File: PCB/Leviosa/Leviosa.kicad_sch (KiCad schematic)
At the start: 48 parts, among them J1 2.54mm 1x03 Servo 1, J2 2.54mm 1x03 Servo 1, J3 2.54mm 1x03 Spare, J4 Barrel_Jack, Q3 TIP122, Q4 TIP122, U1 LM324, U2 ATtiny13A-P, U3 TPS1H200AQDGNRQ1, U5 L7805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

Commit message: Update PCB
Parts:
- Schottky1: renamed from SR206-TPCT-ND1; value Schottky Diode -> Schottky Diode SR206-TPCT-ND1
- renumbered EMcoil1 to Coil1, RV1_10k_Pot1 to Pot1, RV2_10k_Pot1 to Pot2
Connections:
- net at Pot2.1: now also R5.2; no longer R4.1
- net at Pot2.3: now also R4.1; no longer R5.2
- net at R3.2: now also Pot1.3; no longer Pot1.1
- net at R2.1: now also Pot1.1; no longer Pot1.3
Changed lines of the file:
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@@
 	(wire
 		(pts
-			(xy 41.91 38.1) (xy 41.91 39.37)
-		)
-		(stroke
-			(width 0)
-			(type default)
-		)
-	)
-	(wire
-		(pts
 			(xy 219.71 57.15) (xy 245.11 57.15)
 		)
@@
 	(wire
 		(pts
+			(xy 41.91 38.1) (xy 41.91 39.37)
+		)
+		(stroke
+			(width 0)
+			(type default)
+		)
+	)
+	(wire
+		(pts
 			(xy 60.96 55.88) (xy 76.2 55.88)
 		)
@@
 		(lib_id "Device:R_Potentiometer_US")
 		(at 161.29 92.71 0)
+		(mirror x)
 		(unit 1)
 		(exclude_from_sim no)
@@
 		(on_board yes)
 		(dnp no)
-		(property "Reference" "RV2_10k_Pot1"
-			(at 153.162 91.694 0)
+		(property "Reference" "Pot2"
+			(at 153.162 93.726 0)
 			(effects
 				(font
@@
 		)
 		(property "Value" "3362S-1-103LF"
-			(at 151.892 93.98 0)
+			(at 151.892 91.44 0)
 			(effects
 				(font
@@
 			)
 		)
-		(property "Description" ""
-			(at 161.29 92.71 0)
+		(property "Description" "10k pot"
+			(at 166.624 94.234 0)
 			(effects
 				(font
@@
 			(project "Leviosa"
 				(path "/fe766911-203b-467c-b704-d4bd488f6c98"
-					(reference "RV2_10k_Pot1")
+					(reference "Pot2")
 					(unit 1)
 				)
@@
 		(on_board yes)
 		(dnp no)
-		(property "Reference" "SR206-TPCT-ND1"
-			(at 223.52 34.29 90)
+		(property "Reference" "Schottky1"
+			(at 231.648 34.29 90)
 			(effects
 				(font
@@
 			)
 		)
-		(property "Value" "Schottky Diode"
-			(at 226.06 36.83 90)
+		(property "Value" "Schottky Diode SR206-TPCT-ND1"
+			(at 207.772 37.084 90)
 			(effects
 				(font
@@
 			(project "Leviosa"
 				(path "/fe766911-203b-467c-b704-d4bd488f6c98"
-					(reference "SR206-TPCT-ND1")
+					(reference "Schottky1")
 					(unit 1)
 				)
@@
 		(on_board yes)
 		(dnp no)
-		(property "Reference" "EMcoil1"
+		(property "Reference" "Coil1"
 			(at 261.62 34.29 0)
 			(effects
@@
 			(project "Leviosa"
 				(path "/fe766911-203b-467c-b704-d4bd488f6c98"
-					(reference "EMcoil1")
+					(reference "Coil1")
 					(unit 1)
 				)
@@
 		(lib_id "Device:R_Potentiometer_US")
 		(at 161.29 54.61 0)
-		(mirror x)
 		(unit 1)
 		(exclude_from_sim no)
@@
 		(on_board yes)
 		(dnp no)
-		(property "Reference" "RV1_10k_Pot1"
-			(at 152.908 55.372 0)
+		(property "Reference" "Pot1"
+			(at 152.908 53.848 0)
 			(effects
 				(font
@@
 		)
 		(property "Value" "3362S-1-103LF"
-			(at 151.13 53.086 0)
+			(at 151.13 56.134 0)
 			(effects
 				(font
@@
 			)
 		)
-		(property "Description" ""
-			(at 161.29 54.61 0)
+		(property "Description" "10k pot"
+			(at 169.926 53.848 0)
 			(effects
 				(font
@@
 			(project "Leviosa"
 				(path "/fe766911-203b-467c-b704-d4bd488f6c98"
-					(reference "RV1_10k_Pot1")
+					(reference "Pot1")
 					(unit 1)
 				)

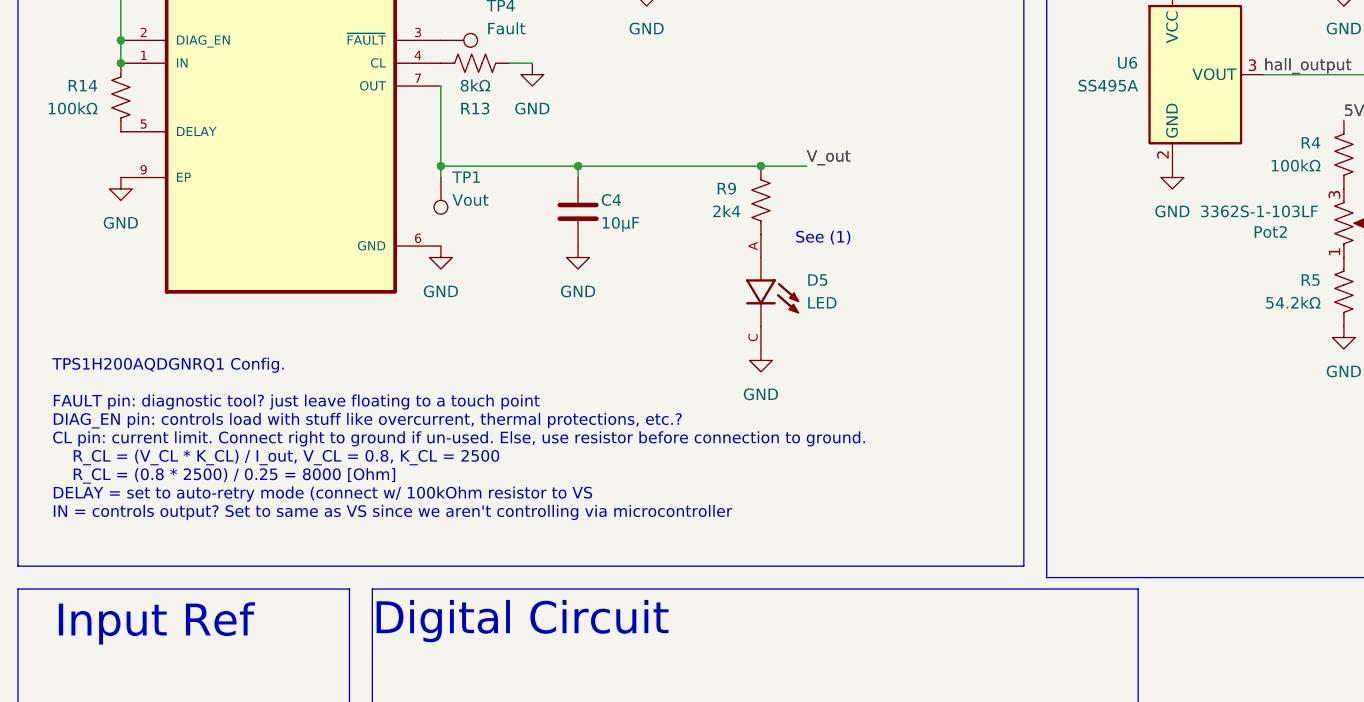
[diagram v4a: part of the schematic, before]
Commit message: Update silkscreen and indicator diodes
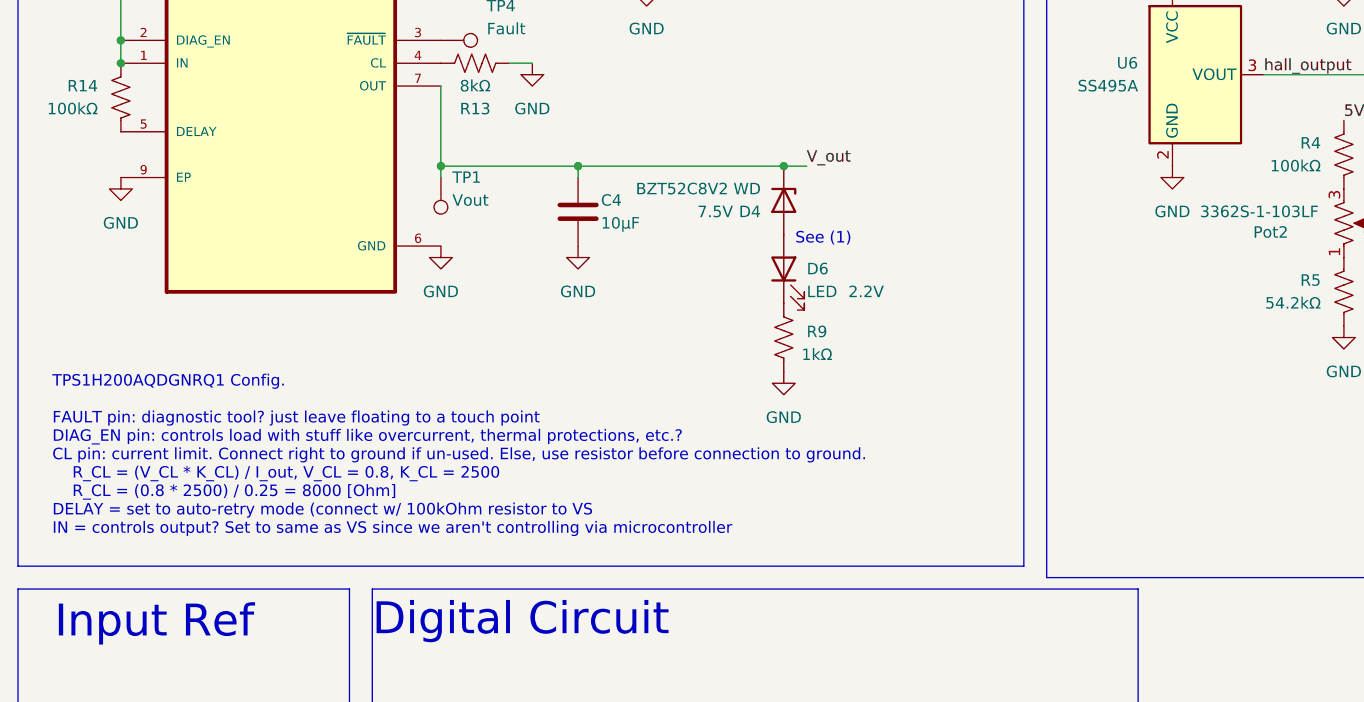
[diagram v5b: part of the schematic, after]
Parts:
- removed D5: LED, MP-2016-1100-50-70:LED_MP-2016-1100-50-70, symbol MP-2016-1100-50-70:MP-2016-1100-50-70
- added D4: BZT52C8V2 WD, Diode_SMD:D_SOD-123, symbol Device:D_Zener
- added D6: LED, LED_SMD:LED_0805_2012Metric, symbol Device:LED
- D2: footprint MP-2016-1100-50-70:LED_MP-2016-1100-50-70 -> LED_SMD:LED_0805_2012Metric
- R9: value 2k4 -> 1kΩ
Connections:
- net GND: now also R9.2
- net V_out: now also D4.1 (K); no longer R9.1
- new net: D6.1 (K), R9.1
- new net: D4.2 (A), D6.2 (A)

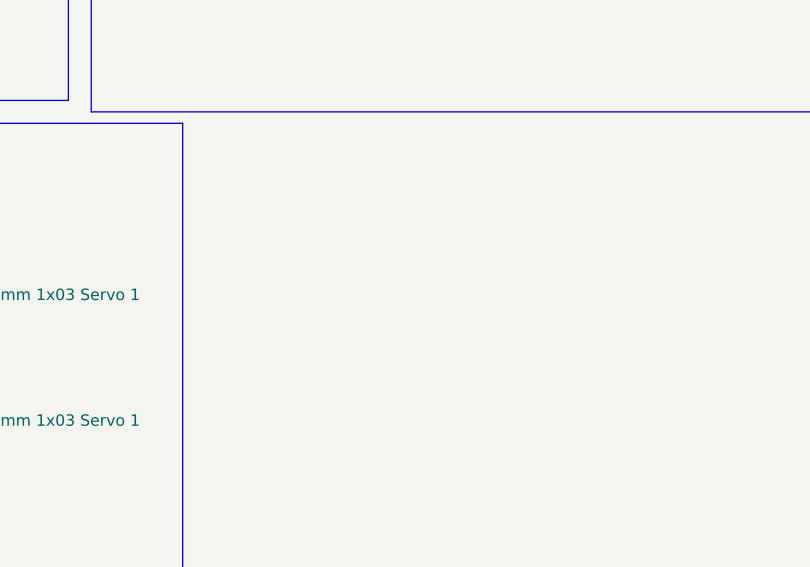
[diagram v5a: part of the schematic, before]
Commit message: add mounting holes
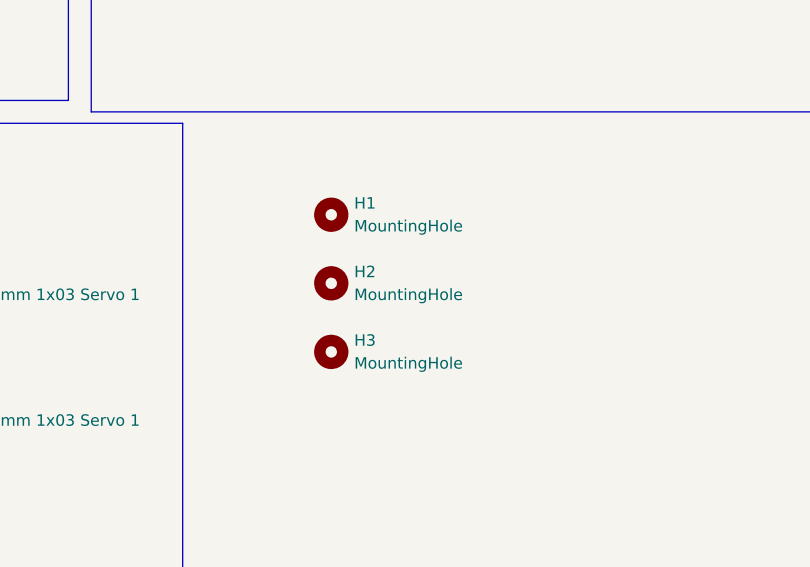
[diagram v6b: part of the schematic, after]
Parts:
- added H1, H2, H3: MountingHole, MountingHole:MountingHole_3.2mm_M3_ISO7380, symbol Mechanical:MountingHole
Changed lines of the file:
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@@
+	)
+	(symbol
+		(lib_id "Mechanical:MountingHole")
+		(at 154.94 158.75 0)
+		(unit 1)
+		(exclude_from_sim no)
+		(in_bom no)
+		(on_board yes)
+		(dnp no)
+		(fields_autoplaced yes)
+		(property "Reference" "H3"
+			(at 157.48 157.4799 0)
+			(effects
+				(font
+					(size 1.27 1.27)
+				)
+				(justify left)
+			)
+		)
+		(property "Value" "MountingHole"
+			(at 157.48 160.0199 0)
+			(effects
+				(font
+					(size 1.27 1.27)
+				)
+				(justify left)
+			)
+		)
+		(property "Footprint" "MountingHole:MountingHole_3.2mm_M3_ISO7380"
+			(at 154.94 158.75 0)
+			(effects
+				(font
+					(size 1.27 1.27)
+				)
+				(hide yes)
+			)
+		)
+		(property "Datasheet" "~"
+			(at 154.94 158.75 0)
+			(effects
+				(font
+					(size 1.27 1.27)
+				)
+				(hide yes)
+			)
+		)
+		(property "Description" "Mounting Hole without connection"
+			(at 154.94 158.75 0)
+			(effects
+				(font
+					(size 1.27 1.27)
+				)
+				(hide yes)
+			)
+		)
+		(instances
+			(project "Leviosa"
+				(path "/fe766911-203b-467c-b704-d4bd488f6c98"
+					(reference "H3")
+					(unit 1)
+				)
+			)
+		)
 	)
 	(symbol
@@
 	)
 	(symbol
+		(lib_id "Mechanical:MountingHole")
+		(at 154.94 143.51 0)
+		(unit 1)
+		(exclude_from_sim no)
+		(in_bom no)
+		(on_board yes)
+		(dnp no)
+		(fields_autoplaced yes)
+		(property "Reference" "H1"
+			(at 157.48 142.2399 0)
+			(effects
+				(font
+					(size 1.27 1.27)
+				)
+				(justify left)
+			)
+		)
+		(property "Value" "MountingHole"
+			(at 157.48 144.7799 0)
+			(effects
+				(font
+					(size 1.27 1.27)
+				)
+				(justify left)
+			)
+		)
+		(property "Footprint" "MountingHole:MountingHole_3.2mm_M3_ISO7380"
+			(at 154.94 143.51 0)
+			(effects
+				(font
+					(size 1.27 1.27)
+				)
+				(hide yes)
+			)
+		)
+		(property "Datasheet" "~"
+			(at 154.94 143.51 0)
+			(effects
+				(font
+					(size 1.27 1.27)
+				)
+				(hide yes)
+			)
+		)
+		(property "Description" "Mounting Hole without connection"
+			(at 154.94 143.51 0)
+			(effects
+				(font
+					(size 1.27 1.27)
+				)
+				(hide yes)
+			)
+		)
+		(instances
+			(project ""
+				(path "/fe766911-203b-467c-b704-d4bd488f6c98"
+					(reference "H1")
+					(unit 1)
+				)
+			)
+		)
+	)
+	(symbol
 		(lib_id "power:GND")
 		(at 73.66 182.88 0)
@@
 					(unit 1)
 				)
+			)
+		)
+	)
+	(symbol
+		(lib_id "Mechanical:MountingHole")
+		(at 154.94 151.13 0)
+		(unit 1)
+		(exclude_from_sim no)
+		(in_bom no)
+		(on_board yes)
+		(dnp no)
+		(fields_autoplaced yes)
+		(property "Reference" "H2"
+			(at 157.48 149.8599 0)
+			(effects
+				(font
+					(size 1.27 1.27)
+				)
+				(justify left)
+			)
+		)
+		(property "Value" "MountingHole"
+			(at 157.48 152.3999 0)
+			(effects
+				(font
+					(size 1.27 1.27)
+				)
+				(justify left)
+			)
+		)
+		(property "Footprint" "MountingHole:MountingHole_3.2mm_M3_ISO7380"
+			(at 154.94 151.13 0)
+			(effects
+				(font
+					(size 1.27 1.27)
+				)
+				(hide yes)
+			)
+		)
+		(property "Datasheet" "~"
+			(at 154.94 151.13 0)
+			(effects
+				(font
+					(size 1.27 1.27)
+				)
+				(hide yes)
+			)
+		)
+		(property "Description" "Mounting Hole without connection"
+			(at 154.94 151.13 0)
+			(effects
+				(font
+					(size 1.27 1.27)
+				)
+				(hide yes)
+			)
+		)
+		(instances
+			(project "Leviosa"
+				(path "/fe766911-203b-467c-b704-d4bd488f6c98"
+					(reference "H2")
+					(unit 1)
+				)
